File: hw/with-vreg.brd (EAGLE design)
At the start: 35.2 x 24.1 mm, 10 parts

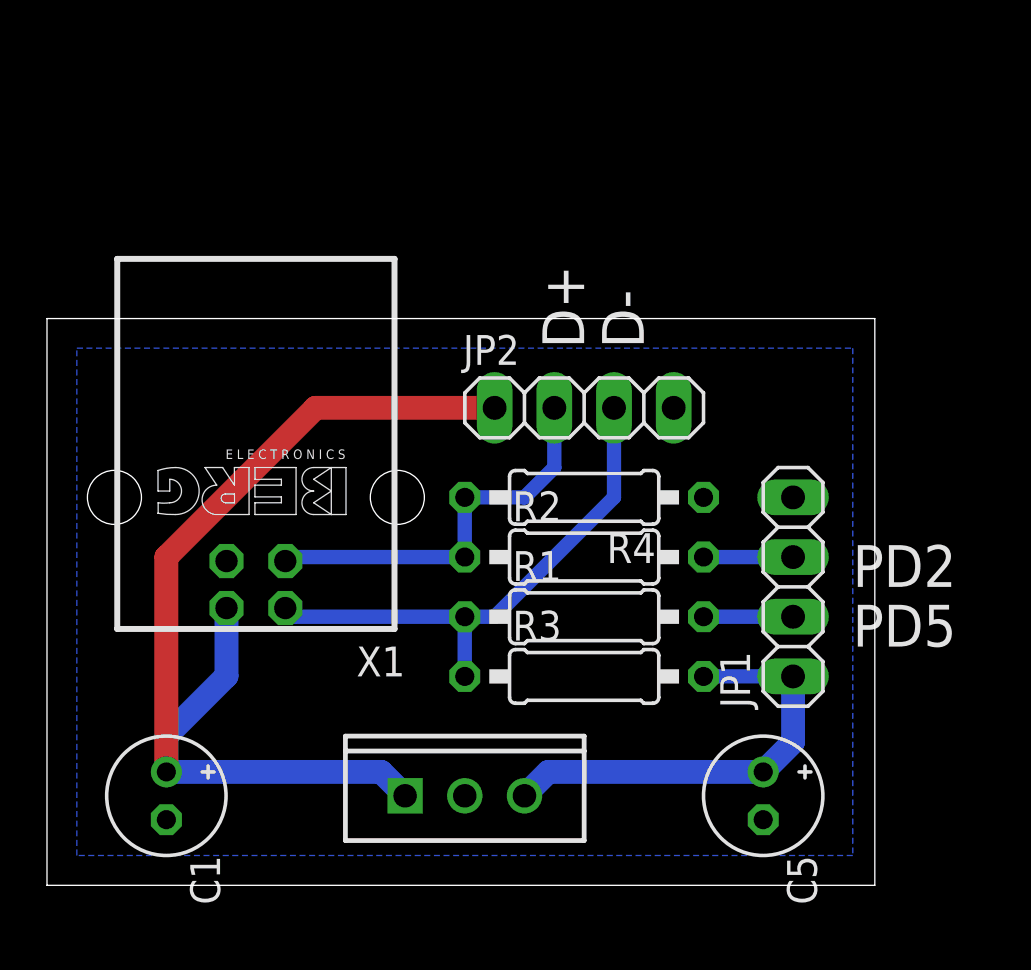
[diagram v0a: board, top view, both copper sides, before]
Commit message: hw: fixed 1k5 pull-up to be controlled by D5
Some lines of errors happened when the 1k5 pull-up from `D-`
wired directly to 3V3.

Think it caused by boot delay of Arduino.
Anyway, the errors can be removed by wire the pull-up to D5 and,
let UsbKeyboard control it.

Signed-off-by: Homin Lee <homin.lee@suapapa.net>
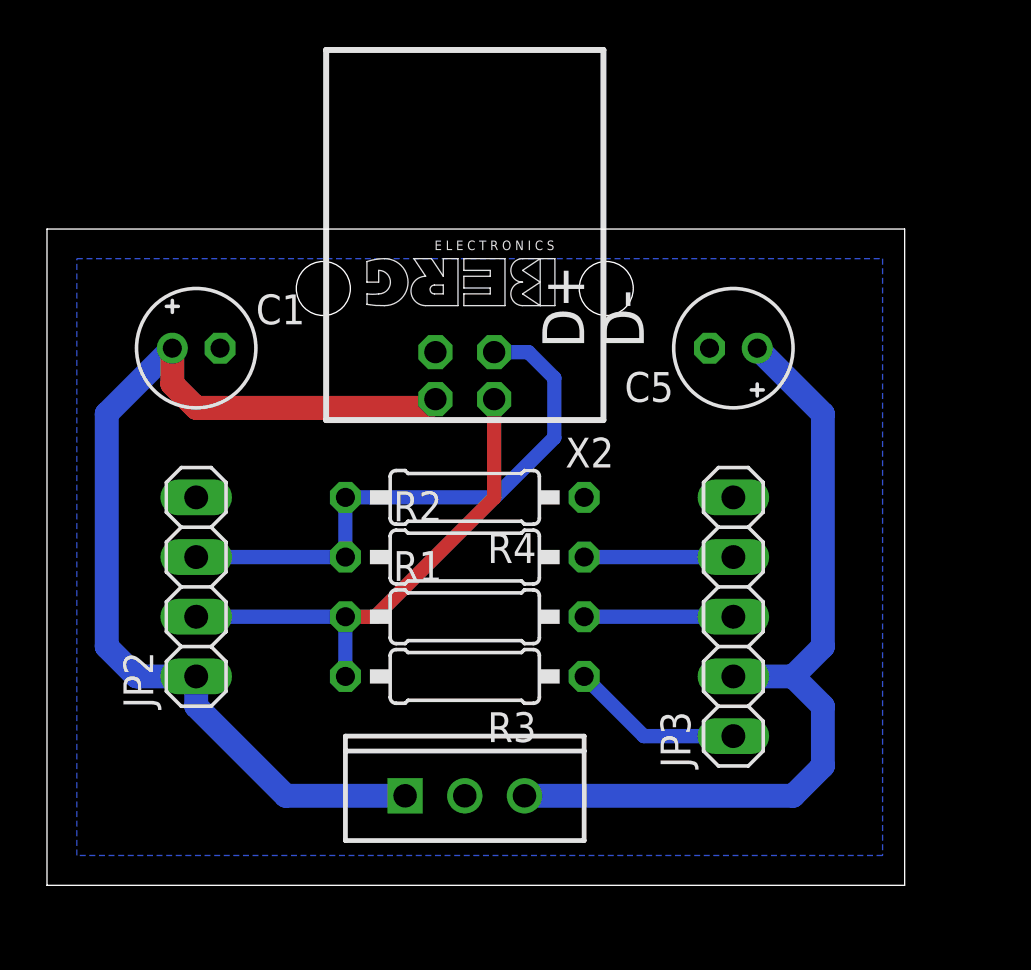
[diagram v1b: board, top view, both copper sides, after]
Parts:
- removed JP1: (no value), pinhead:1X04
- removed X1: (no value), con-berg:PN61729
- added JP3: (no value), pinhead:1X05
- added X2: (no value), con-berg:PN61729
- moved C1 19.1 mm to (6.35, 22.9), turned to 0 degrees
- moved C5 19.1 mm to (29.2, 22.9), turned to 180 degrees
- moved JP2 18.2 mm to (6.35, 12.7), turned to 90 degrees
- moved R1 5.08 mm to (17.8, 11.4)
- moved R2 5.08 mm to (17.8, 14.0)
- moved R3 5.08 mm to (17.8, 8.89), turned to 180 degrees
- moved R4 5.08 mm to (17.8, 16.5)
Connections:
- new net N$4: JP3.1, R3.1
- net D+: now also JP2.3, X2.3; no longer JP2.2, X1.3
- net D-: now also JP2.2, R3.2, X2.2; no longer JP2.3, R3.1, X1.2
- net GND: now also JP3.5, X2.4; no longer JP1.4, X1.4
- net N$1: now also JP3.3; no longer JP1.2
- net N$2: now also JP3.4; no longer JP1.3
- net N$3: now also X2.1; no longer X1.1
- net VCC: now also JP3.2; no longer JP1.1, R3.2
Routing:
- net VCC: track 19.0 -> 35.8 mm
- net N$4: track 0.00 -> 7.40 mm
- net D+: track 17.1 -> 24.4 mm
- net N$2: track 3.81 -> 6.35 mm
- net N$1: track 3.81 -> 6.35 mm
- net N$3: track 44.4 -> 43.2 mm
- net D-: track 22.6 -> 21.5 mm
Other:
- board size 35.2 x 24.1 mm -> 36.5 x 27.9 mm
- board text added: "D2"
- board text added: "D4"
- board text added: "D5"
- board text added: "G"
- board text added: "V"
- board text removed: "PD2"
- board text removed: "PD5"
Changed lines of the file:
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@@
 <board>
 <plain>
-<wire x1="0" y1="0" x2="35.23" y2="0" width="0" layer="20"/>
-<wire x1="35.23" y1="0" x2="35.23" y2="24.12" width="0" layer="20"/>
-<wire x1="35.23" y1="24.12" x2="0" y2="24.12" width="0" layer="20"/>
-<wire x1="0" y1="24.12" x2="0" y2="0" width="0" layer="20"/>
-<text x="34.29" y="12.7" size="1.778" layer="25" font="vector">PD2</text>
-<text x="34.29" y="10.16" size="1.778" layer="25" font="vector">PD5</text>
+<wire x1="0" y1="0" x2="36.5" y2="0" width="0" layer="20"/>
+<wire x1="36.5" y1="0" x2="36.5" y2="27.93" width="0" layer="20"/>
+<wire x1="36.5" y1="27.93" x2="0" y2="27.93" width="0" layer="20"/>
+<wire x1="0" y1="27.93" x2="0" y2="0" width="0" layer="20"/>
 <text x="25.4" y="22.86" size="1.778" layer="25" font="vector" rot="R90">D-</text>
 <text x="22.86" y="22.86" size="1.778" layer="25" font="vector" rot="R90">D+</text>
+<text x="31.75" y="5.08" size="1.778" layer="27" font="vector">D5</text>
+<text x="31.75" y="7.62" size="1.778" layer="27" font="vector">V</text>
+<text x="31.75" y="10.16" size="1.778" layer="27" font="vector">D4</text>
+<text x="31.75" y="12.7" size="1.778" layer="27" font="vector">D2</text>
+<text x="31.75" y="15.24" size="1.778" layer="27" font="vector">G</text>
 </plain>
 <attributes>
@@
 </autorouter>
 <elements>
-<element name="X1" library="con-berg" package="PN61729" value="" x="8.89" y="16.51" rot="R180"/>
-<element name="R1" library="rcl" package="0207/10" value="68R" x="22.86" y="11.43"/>
-<element name="R2" library="rcl" package="0207/10" value="68R" x="22.86" y="13.97"/>
-<element name="R3" library="rcl" package="0207/10" value="1k5" x="22.86" y="8.89"/>
-<element name="C1" library="rcl" package="E2-5" value="4u7" x="5.08" y="3.81" rot="R270"/>
-<element name="R4" library="rcl" package="0207/10" value="1M" x="22.86" y="16.51" rot="R180"/>
-<element name="C5" library="rcl" package="E2-5" value="4u7" x="30.48" y="3.81" rot="R270"/>
-<element name="JP1" library="pinhead" package="1X04" value="" x="31.75" y="12.7" rot="R90"/>
+<element name="R1" library="rcl" package="0207/10" value="68R" x="17.78" y="11.43"/>
+<element name="R2" library="rcl" package="0207/10" value="68R" x="17.78" y="13.97"/>
+<element name="R3" library="rcl" package="0207/10" value="1k5" x="17.78" y="8.89" rot="R180"/>
+<element name="C1" library="rcl" package="E2-5" value="4u7" x="6.35" y="22.86"/>
+<element name="R4" library="rcl" package="0207/10" value="1M" x="17.78" y="16.51" rot="R180"/>
+<element name="C5" library="rcl" package="E2-5" value="4u7" x="29.21" y="22.86" rot="R180"/>
 <element name="IC1" library="SparkFun" package="TO220-IGO" value="" x="17.78" y="3.81"/>
-<element name="JP2" library="pinhead" package="1X04" value="" x="22.86" y="20.32"/>
+<element name="JP2" library="pinhead" package="1X04" value="" x="6.35" y="12.7" rot="R90"/>
+<element name="JP3" library="pinhead" package="1X05" value="" x="29.21" y="11.43" rot="R90"/>
+<element name="X2" library="con-berg" package="PN61729" value="" x="17.78" y="25.4" rot="R180"/>
 </elements>
 <signals>
 <signal name="GND">
 <contactref element="C1" pad="-"/>
-<contactref element="X1" pad="4"/>
-<contactref element="C5" pad="-"/>
-<contactref element="R4" pad="1"/>
-<contactref element="JP1" pad="4"/>
-<contactref element="IC1" pad="GND"/>
 <polygon width="0.4064" layer="16">
-<vertex x="1.27" y="22.86"/>
-<vertex x="34.29" y="22.86"/>
-<vertex x="34.29" y="1.27"/>
+<vertex x="1.27" y="26.67"/>
+<vertex x="35.56" y="26.67"/>
+<vertex x="35.56" y="1.27"/>
 <vertex x="1.27" y="1.27"/>
 </polygon>
 <contactref element="JP2" pad="4"/>
+<contactref element="X2" pad="4"/>
+<contactref element="IC1" pad="GND"/>
+<contactref element="C5" pad="-"/>
+<contactref element="R4" pad="1"/>
+<contactref element="JP3" pad="5"/>
 </signal>
 <signal name="VCC">
-<contactref element="R3" pad="2"/>
 <contactref element="C5" pad="+"/>
-<contactref element="JP1" pad="1"/>
 <contactref element="IC1" pad="OUT"/>
-<wire x1="20.32" y1="3.81" x2="21.336" y2="4.826" width="1.016" layer="16"/>
-<wire x1="21.336" y1="4.826" x2="30.48" y2="4.826" width="1.016" layer="16"/>
-<wire x1="30.48" y1="4.826" x2="31.75" y2="6.096" width="1.016" layer="16"/>
-<wire x1="31.75" y1="6.096" x2="31.75" y2="8.89" width="1.016" layer="16"/>
-<wire x1="27.94" y1="8.89" x2="31.75" y2="8.89" width="0.6096" layer="16"/>
+<contactref element="JP3" pad="2"/>
+<wire x1="20.32" y1="3.81" x2="31.75" y2="3.81" width="1.016" layer="16"/>
+<wire x1="31.75" y1="3.81" x2="33.02" y2="5.08" width="1.016" layer="16"/>
+<wire x1="33.02" y1="5.08" x2="33.02" y2="7.62" width="1.016" layer="16"/>
+<wire x1="33.02" y1="7.62" x2="31.75" y2="8.89" width="1.016" layer="16"/>
+<wire x1="31.75" y1="8.89" x2="29.21" y2="8.89" width="1.016" layer="16"/>
+<wire x1="30.226" y1="22.86" x2="33.02" y2="20.066" width="1.016" layer="16"/>
+<wire x1="33.02" y1="20.066" x2="33.02" y2="10.16" width="1.016" layer="16"/>
+<wire x1="33.02" y1="10.16" x2="31.75" y2="8.89" width="1.016" layer="16"/>
 </signal>
 <signal name="D-">
 <contactref element="R1" pad="1"/>
-<contactref element="X1" pad="2"/>
-<contactref element="R3" pad="1"/>
-<wire x1="10.14" y1="11.8" x2="10.51" y2="11.43" width="0.6096" layer="16"/>
-<wire x1="10.51" y1="11.43" x2="17.78" y2="11.43" width="0.6096" layer="16"/>
-<wire x1="17.78" y1="11.43" x2="17.78" y2="8.89" width="0.6096" layer="16"/>
-<contactref element="JP2" pad="3"/>
-<wire x1="17.78" y1="11.43" x2="19.05" y2="11.43" width="0.6096" layer="16"/>
-<wire x1="19.05" y1="11.43" x2="24.13" y2="16.51" width="0.6096" layer="16"/>
-<wire x1="24.13" y1="16.51" x2="24.13" y2="20.32" width="0.6096" layer="16"/>
+<contactref element="R3" pad="2"/>
+<contactref element="JP2" pad="2"/>
+<contactref element="X2" pad="2"/>
+<wire x1="12.7" y1="11.43" x2="6.35" y2="11.43" width="0.6096" layer="16"/>
+<wire x1="12.7" y1="11.43" x2="12.7" y2="8.89" width="0.6096" layer="16"/>
+<wire x1="19.03" y1="20.69" x2="19.03" y2="16.49" width="0.6096" layer="1"/>
+<wire x1="19.03" y1="16.49" x2="13.97" y2="11.43" width="0.6096" layer="1"/>
+<wire x1="13.97" y1="11.43" x2="12.7" y2="11.43" width="0.6096" layer="1"/>
 </signal>
 <signal name="D+">
-<contactref element="X1" pad="3"/>
 <contactref element="R2" pad="1"/>
 <contactref element="R4" pad="2"/>
-<wire x1="17.78" y1="13.97" x2="10.31" y2="13.97" width="0.6096" layer="16"/>
-<wire x1="10.31" y1="13.97" x2="10.14" y2="13.8" width="0.6096" layer="16"/>
-<wire x1="17.78" y1="13.97" x2="17.78" y2="16.51" width="0.6096" layer="16"/>
-<contactref element="JP2" pad="2"/>
-<wire x1="21.59" y1="20.32" x2="21.59" y2="17.78" width="0.6096" layer="16"/>
-<wire x1="21.59" y1="17.78" x2="20.32" y2="16.51" width="0.6096" layer="16"/>
-<wire x1="20.32" y1="16.51" x2="17.78" y2="16.51" width="0.6096" layer="16"/>
+<wire x1="12.7" y1="13.97" x2="12.7" y2="16.51" width="0.6096" layer="16"/>
+<wire x1="19.05" y1="16.51" x2="12.7" y2="16.51" width="0.6096" layer="16"/>
+<contactref element="JP2" pad="3"/>
+<contactref element="X2" pad="3"/>
+<wire x1="12.7" y1="13.97" x2="6.35" y2="13.97" width="0.6096" layer="16"/>
+<wire x1="19.05" y1="16.51" x2="21.59" y2="19.05" width="0.6096" layer="16"/>
+<wire x1="19.03" y1="22.69" x2="20.49" y2="22.69" width="0.6096" layer="16"/>
+<wire x1="20.49" y1="22.69" x2="21.59" y2="21.59" width="0.6096" layer="16"/>
+<wire x1="21.59" y1="21.59" x2="21.59" y2="19.05" width="0.6096" layer="16"/>
 </signal>
 <signal name="N$3">
 <contactref element="C1" pad="+"/>
-<contactref element="X1" pad="1"/>
 <contactref element="IC1" pad="IN"/>
 <contactref element="JP2" pad="1"/>
-<wire x1="7.64" y1="11.8" x2="7.64" y2="8.91" width="1.016" layer="16"/>
-<wire x1="7.64" y1="8.91" x2="5.08" y2="6.35" width="1.016" layer="16"/>
-<wire x1="5.08" y1="6.35" x2="5.08" y2="4.826" width="1.016" layer="16"/>
-<wire x1="5.08" y1="4.826" x2="14.224" y2="4.826" width="1.016" layer="16"/>
-<wire x1="14.224" y1="4.826" x2="15.24" y2="3.81" width="1.016" layer="16"/>
-<wire x1="19.05" y1="20.32" x2="11.43" y2="20.32" width="1.016" layer="1"/>
-<wire x1="11.43" y1="20.32" x2="5.08" y2="13.97" width="1.016" layer="1"/>
-<wire x1="5.08" y1="13.97" x2="5.08" y2="4.826" width="1.016" layer="1"/>
+<contactref element="X2" pad="1"/>
+<wire x1="15.24" y1="3.81" x2="10.16" y2="3.81" width="1.016" layer="16"/>
+<wire x1="10.16" y1="3.81" x2="6.35" y2="7.62" width="1.016" layer="16"/>
+<wire x1="6.35" y1="7.62" x2="6.35" y2="8.89" width="1.016" layer="16"/>
+<wire x1="5.334" y1="22.86" x2="5.334" y2="21.336" width="1.016" layer="1"/>
+<wire x1="5.334" y1="21.336" x2="6.35" y2="20.32" width="1.016" layer="1"/>
+<wire x1="6.35" y1="20.32" x2="16.16" y2="20.32" width="1.016" layer="1"/>
+<wire x1="16.16" y1="20.32" x2="16.53" y2="20.69" width="1.016" layer="1"/>
+<wire x1="6.35" y1="8.89" x2="3.81" y2="8.89" width="1.016" layer="16"/>
+<wire x1="3.81" y1="8.89" x2="2.54" y2="10.16" width="1.016" layer="16"/>
+<wire x1="2.54" y1="10.16" x2="2.54" y2="20.066" width="1.016" layer="16"/>
+<wire x1="2.54" y1="20.066" x2="5.334" y2="22.86" width="1.016" layer="16"/>
 </signal>
 <signal name="N$1">
 <contactref element="R1" pad="2"/>
-<contactref element="JP1" pad="2"/>
-<wire x1="27.94" y1="11.43" x2="31.75" y2="11.43" width="0.6096" layer="16"/>
+<contactref element="JP3" pad="3"/>
+<wire x1="22.86" y1="11.43" x2="29.21" y2="11.43" width="0.6096" layer="16"/>
 </signal>
 <signal name="N$2">
 <contactref element="R2" pad="2"/>
-<contactref element="JP1" pad="3"/>
-<wire x1="27.94" y1="13.97" x2="31.75" y2="13.97" width="0.6096" layer="16"/>
+<contactref element="JP3" pad="4"/>
+<wire x1="22.86" y1="13.97" x2="29.21" y2="13.97" width="0.6096" layer="16"/>
+</signal>
+<signal name="N$4">
+<contactref element="R3" pad="1"/>
+<contactref element="JP3" pad="1"/>
+<wire x1="22.86" y1="8.89" x2="25.4" y2="6.35" width="0.6096" layer="16"/>
+<wire x1="25.4" y1="6.35" x2="29.21" y2="6.35" width="0.6096" layer="16"/>
 </signal>
 </signals>
